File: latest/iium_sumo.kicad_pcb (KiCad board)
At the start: 2 copper layers, 101.3 x 62.2 mm, 60 parts, among them J1 I2C_VL53_1, J10 Cytron MD, J11 Cytron Start Module, J12 Conn_01x04, J13 Conn_01x04, J14 Conn_01x04, J15 EXTRA1, J16 Conn_01x02_Pin, J17 Conn_01x02_Pin, J18 UART1, J19 UART2, J2 I2C_VL53_2, J3 I2C_VL53_3, J4 I2C_VL53_4, J5 I2C_VL53_5, J6 IR_1, J7 IR_2, J8 IR_3, J9 IR_4, SW1 SW_SPST, SW2 SW_SPST, U1 TPS54360DDA, U4 Black Pill v2, U5 LM3940

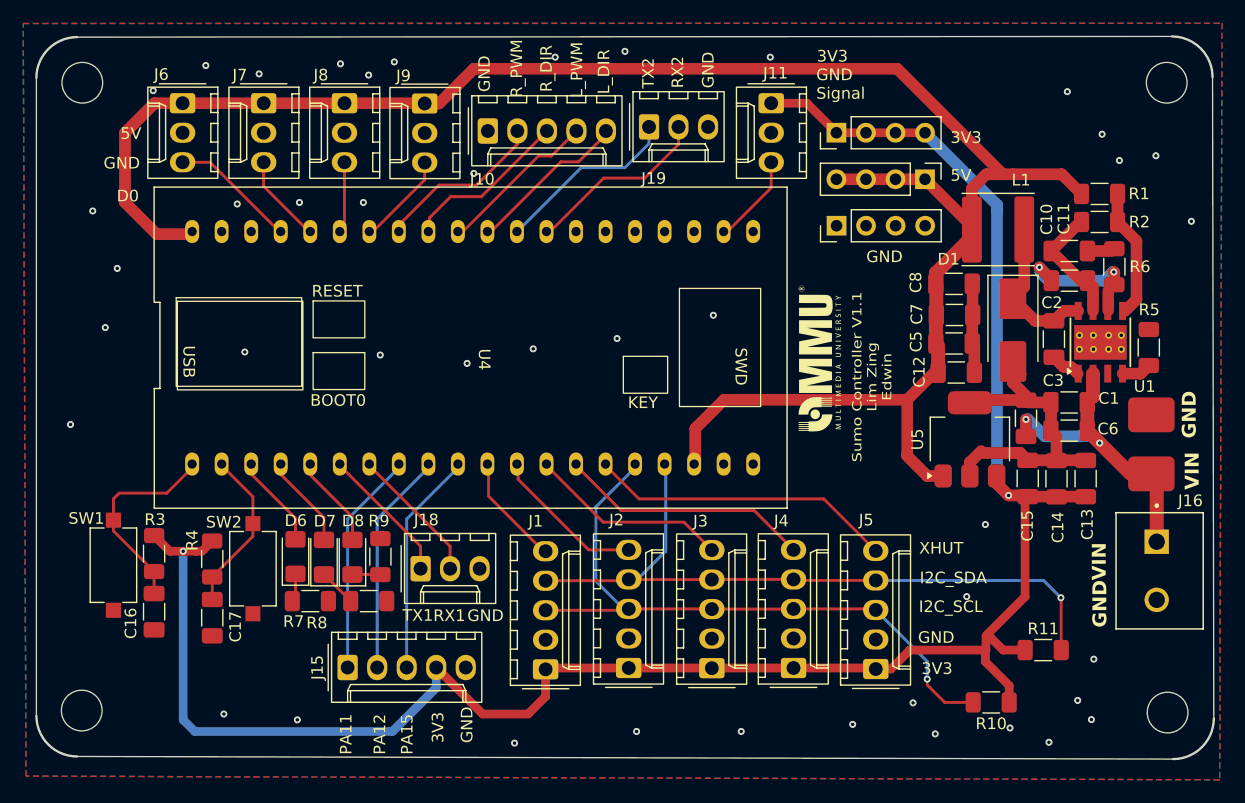
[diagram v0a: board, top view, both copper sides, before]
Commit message: Added Labels
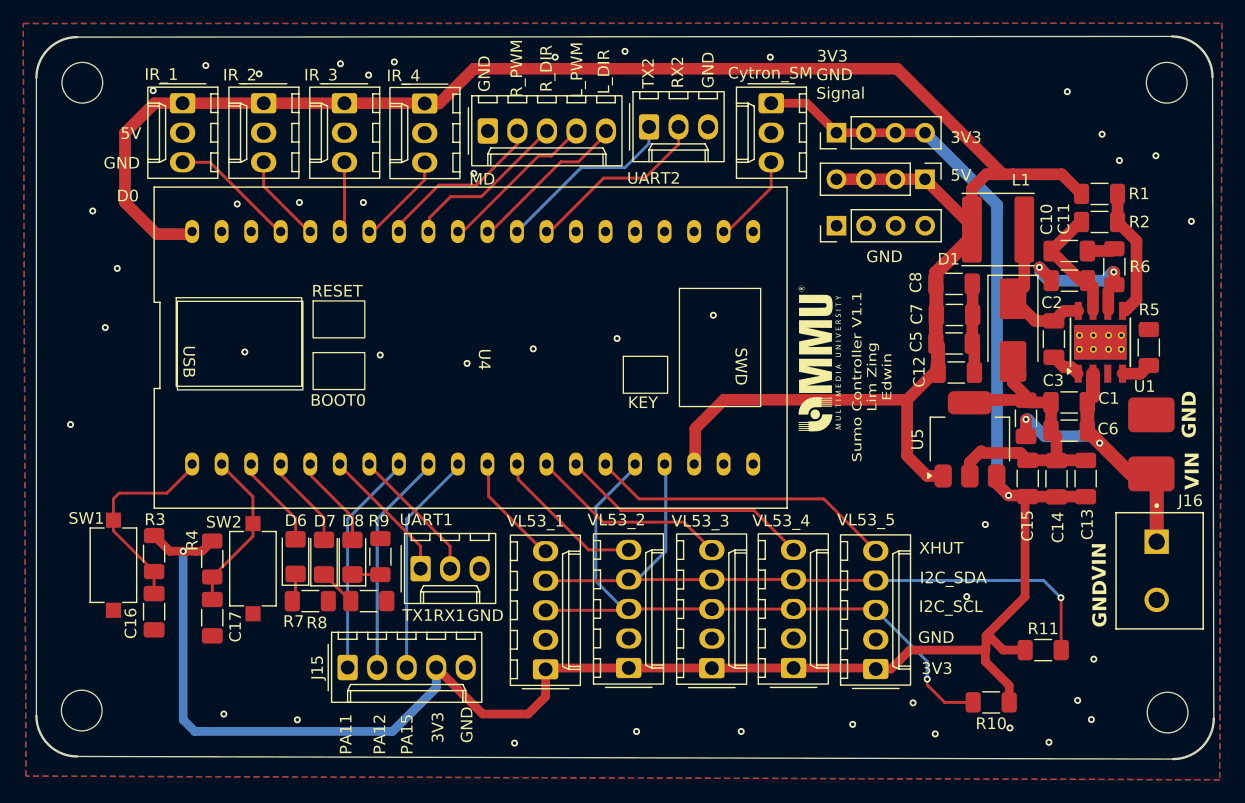
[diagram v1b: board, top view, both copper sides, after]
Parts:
- renumbered J11 to Cytron_SM, J6 to IR_1, J7 to IR_2, J8 to IR_3, J9 to IR_4, J10 to MD, J18 to UART1, J19 to UART2, J1 to VL53_1, J2 to VL53_2, J3 to VL53_3, J4 to VL53_4, J5 to VL53_5

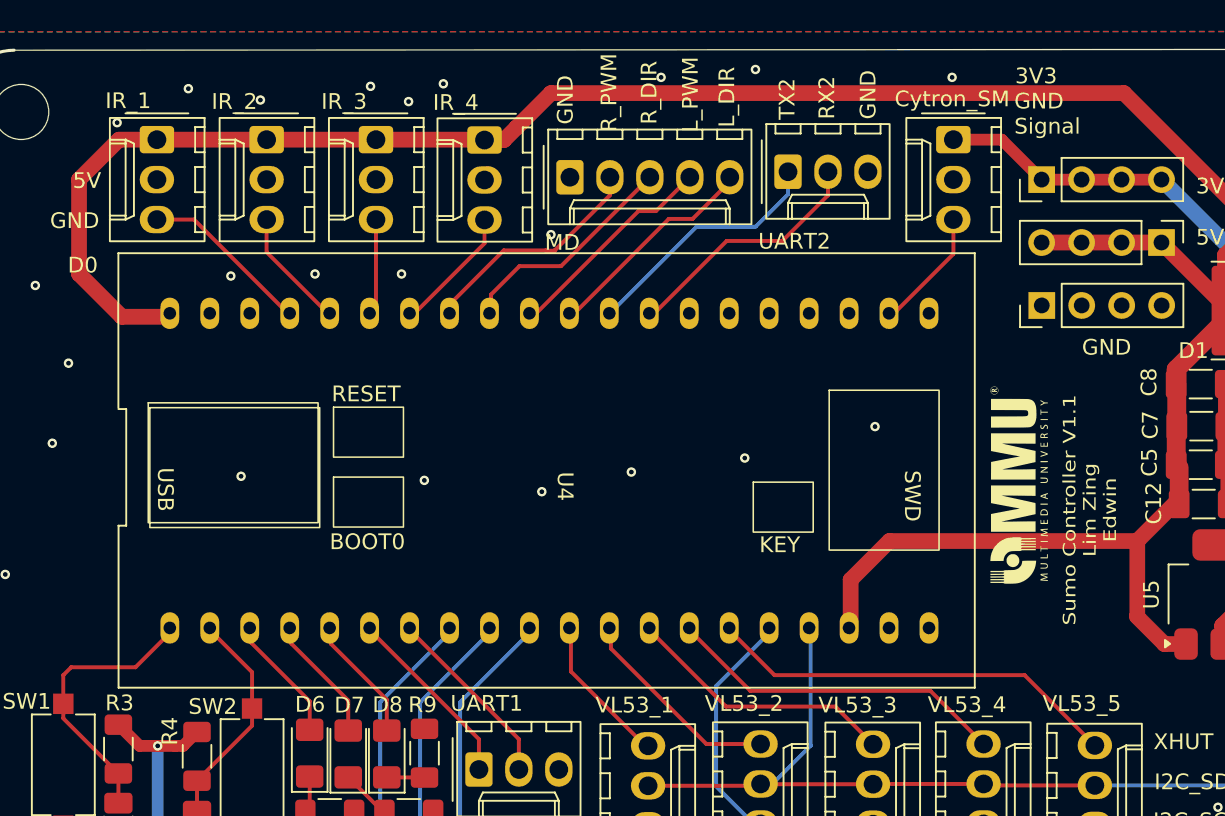
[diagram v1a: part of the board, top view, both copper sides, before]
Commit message: Updated pull resisto
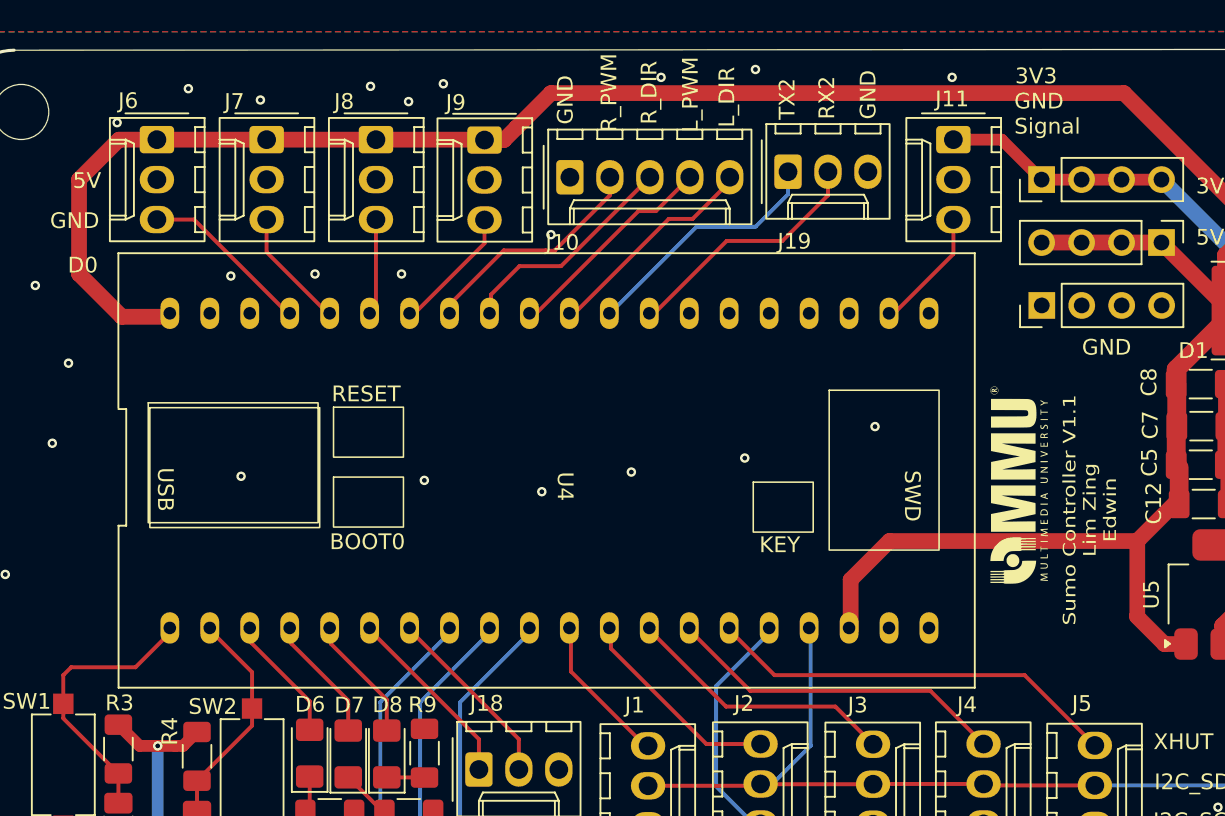
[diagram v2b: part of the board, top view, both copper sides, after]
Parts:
- R10, R11: value 4k -> 4.7k
- renumbered VL53_1 to J1, MD to J10, Cytron_SM to J11, UART1 to J18, UART2 to J19, VL53_2 to J2, VL53_3 to J3, VL53_4 to J4, VL53_5 to J5, IR_1 to J6, IR_2 to J7, IR_3 to J8, IR_4 to J9
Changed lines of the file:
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@@
 		(descr "Molex KK-254 Interconnect System, old/engineering part number: AE-6410-03A example for new part number: 22-27-2031, 3 Pins (http://www.molex.com/pdm_docs/sd/022272021_sd.pdf)")
 		(tags "connector Molex KK-254 vertical")
-		(property "Reference" "Cytron_SM"
+		(property "Reference" "J11"
 			(at -2.585 0.08 180)
 			(layer "F.SilkS")
@@
 		(descr "Molex KK-254 Interconnect System, old/engineering part number: AE-6410-05A example for new part number: 22-27-2051, 5 Pins (http://www.molex.com/pdm_docs/sd/022272021_sd.pdf)")
 		(tags "connector Molex KK-254 vertical")
-		(property "Reference" "VL53_2"
+		(property "Reference" "J2"
 			(at 12.73 -1.05 180)
 			(layer "F.SilkS")
@@
 		(descr "Molex KK-254 Interconnect System, old/engineering part number: AE-6410-05A example for new part number: 22-27-2051, 5 Pins (http://www.molex.com/pdm_docs/sd/022272021_sd.pdf)")
 		(tags "connector Molex KK-254 vertical")
-		(property "Reference" "VL53_3"
+		(property "Reference" "J3"
 			(at 12.645 -0.975 180)
 			(layer "F.SilkS")
@@
 			)
 		)
-		(property "Value" "4k"
+		(property "Value" "4.7k"
 			(at 0 1.83 0)
 			(layer "F.Fab")
@@
 		(descr "Molex KK-254 Interconnect System, old/engineering part number: AE-6410-05A example for new part number: 22-27-2051, 5 Pins (http://www.molex.com/pdm_docs/sd/022272021_sd.pdf)")
 		(tags "connector Molex KK-254 vertical")
-		(property "Reference" "VL53_1"
+		(property "Reference" "J1"
 			(at 12.745 -0.85 180)
 			(layer "F.SilkS")
@@
 		(descr "Molex KK-254 Interconnect System, old/engineering part number: AE-6410-05A example for new part number: 22-27-2051, 5 Pins (http://www.molex.com/pdm_docs/sd/022272021_sd.pdf)")
 		(tags "connector Molex KK-254 vertical")
-		(property "Reference" "VL53_5"
+		(property "Reference" "J5"
 			(at 12.82 -0.825 180)
 			(layer "F.SilkS")
@@
 			)
 		)
-		(property "Value" "4k"
+		(property "Value" "4.7k"
 			(at 0 1.83 0)
 			(layer "F.Fab")
@@
 		(descr "Molex KK-254 Interconnect System, old/engineering part number: AE-6410-05A example for new part number: 22-27-2051, 5 Pins (http://www.molex.com/pdm_docs/sd/022272021_sd.pdf)")
 		(tags "connector Molex KK-254 vertical")
-		(property "Reference" "MD"
+		(property "Reference" "J10"
 			(at -0.48 4.15 180)
 			(layer "F.SilkS")
@@
 		(descr "Molex KK-254 Interconnect System, old/engineering part number: AE-6410-03A example for new part number: 22-27-2031, 3 Pins (http://www.molex.com/pdm_docs/sd/022272021_sd.pdf)")
 		(tags "connector Molex KK-254 vertical")
-		(property "Reference" "IR_1"
+		(property "Reference" "J6"
 			(at -2.47 1.825 180)
 			(layer "F.SilkS")
@@
 		(descr "Molex KK-254 Interconnect System, old/engineering part number: AE-6410-03A example for new part number: 22-27-2031, 3 Pins (http://www.molex.com/pdm_docs/sd/022272021_sd.pdf)")
 		(tags "connector Molex KK-254 vertical")
-		(property "Reference" "UART1"
+		(property "Reference" "J18"
 			(at 0.49 -4.2 0)
 			(layer "F.SilkS")
@@
 		(descr "Molex KK-254 Interconnect System, old/engineering part number: AE-6410-03A example for new part number: 22-27-2031, 3 Pins (http://www.molex.com/pdm_docs/sd/022272021_sd.pdf)")
 		(tags "connector Molex KK-254 vertical")
-		(property "Reference" "IR_2"
+		(property "Reference" "J7"
 			(at -2.42 2.05 180)
 			(layer "F.SilkS")
@@
 		(descr "Molex KK-254 Interconnect System, old/engineering part number: AE-6410-03A example for new part number: 22-27-2031, 3 Pins (http://www.molex.com/pdm_docs/sd/022272021_sd.pdf)")
 		(tags "connector Molex KK-254 vertical")
-		(property "Reference" "IR_4"
+		(property "Reference" "J9"
 			(at -2.38 1.825 0)
 			(layer "F.SilkS")
@@
 		(descr "Molex KK-254 Interconnect System, old/engineering part number: AE-6410-03A example for new part number: 22-27-2031, 3 Pins (http://www.molex.com/pdm_docs/sd/022272021_sd.pdf)")
 		(tags "connector Molex KK-254 vertical")
-		(property "Reference" "IR_3"
+		(property "Reference" "J8"
 			(at -2.42 2.025 180)
 			(layer "F.SilkS")
@@
 		(descr "Molex KK-254 Interconnect System, old/engineering part number: AE-6410-05A example for new part number: 22-27-2051, 5 Pins (http://www.molex.com/pdm_docs/sd/022272021_sd.pdf)")
 		(tags "connector Molex KK-254 vertical")
-		(property "Reference" "VL53_4"
+		(property "Reference" "J4"
 			(at 12.655 -1.05 180)
 			(layer "F.SilkS")
@@
 		(descr "Molex KK-254 Interconnect System, old/engineering part number: AE-6410-03A example for new part number: 22-27-2031, 3 Pins (http://www.molex.com/pdm_docs/sd/022272021_sd.pdf)")
 		(tags "connector Molex KK-254 vertical")
-		(property "Reference" "UART2"
+		(property "Reference" "J19"
 			(at 0.405 4.425 0)
 			(layer "F.SilkS")

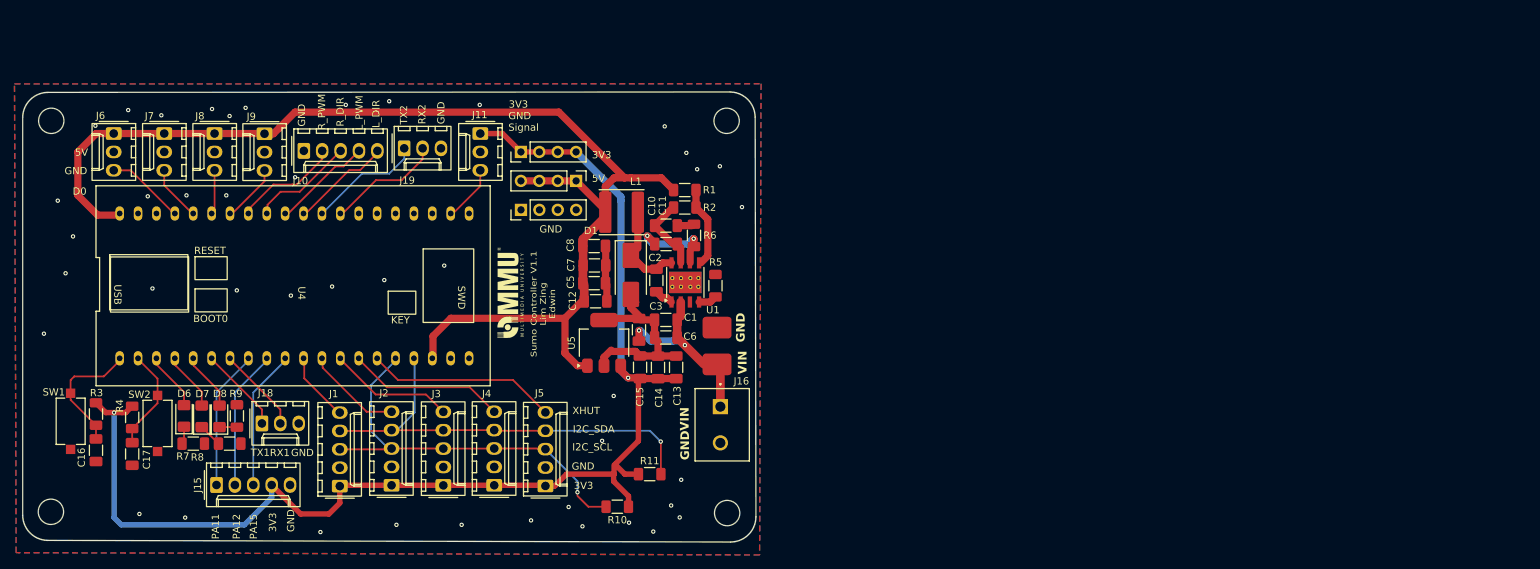
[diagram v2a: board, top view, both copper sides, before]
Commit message: pcb update and rearrange
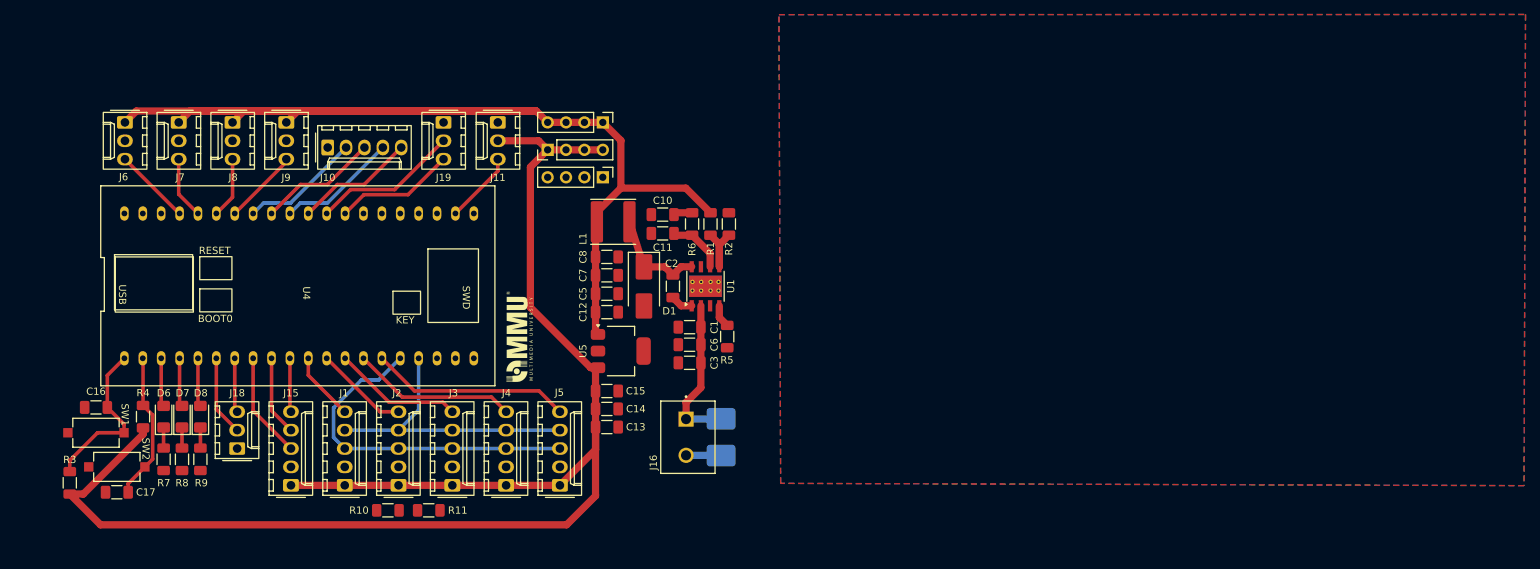
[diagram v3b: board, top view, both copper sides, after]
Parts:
- removed REF** (x4): MountingHole_3.5mm, MountingHole:MountingHole_3.5mm
- J17: moved to B.Cu
- moved R10 31.7 mm to (146.8, 118.0), turned to 0 degrees
- moved R11 30.9 mm to (152.5, 118.0), turned to 180 degrees
- moved C13 12.6 mm to (177.1, 106.5), turned to 0 degrees
- moved J14 12.2 mm to (176.5, 72.0), turned to -90 degrees
- moved J15 10.3 mm to (133.4, 114.5), turned to 90 degrees
- moved R3 10.2 mm to (102.9, 114.2), turned to 90 degrees
- moved C14 9.09 mm to (177.1, 104.0), turned to 0 degrees
- moved J13 8.88 mm to (176.5, 64.4)
- moved C3 8.35 mm to (188.5, 97.6), turned to 180 degrees
- moved SW2 8.22 mm to (109.4, 112.0), turned to 180 degrees
- moved R9 7.83 mm to (120.9, 111.0), turned to 90 degrees
- moved J17 7.54 mm to (192.8, 105.4), turned to -90 degrees
- moved R5 7.21 mm to (193.7, 94.0), turned to -90 degrees
- moved R8 6.93 mm to (118.4, 111.0), turned to 90 degrees
- moved R2 6.51 mm to (193.9, 78.5), turned to 90 degrees
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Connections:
- J11 pad 1: +3V3 -> GND
- J11 pad 2: GND -> +3V3
- J15 pad 1: /PA11 -> +3V3
- J15 pad 2: /PA12 -> GND
- J15 pad 3: /PA15 -> /PA11
- J15 pad 4: +3V3 -> /PA12
- J15 pad 5: GND -> /PA15
- J18 pad 1: /TX1 -> GND
- J18 pad 2: /RX1 -> /TX1
- J18 pad 3: GND -> /RX1
- J19 pad 1: /TX2 -> GND
- J19 pad 2: /RX2 -> /TX2
- J19 pad 3: GND -> /RX2
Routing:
- net +5V: track 170.8 -> 240.8 mm
- net GND: track 50.1 -> 4.85 mm, vias 43 -> 0
- net +3V3: track 180.3 -> 206.5 mm, vias 2 -> 0
- net /I2C_SDA: track 61.1 -> 41.1 mm, vias 1 -> 0
- net /PA15: track 19.1 -> 7.44 mm
- net /I2C_SCL: track 56.5 -> 48.0 mm, vias 1 -> 0
- net /PA12: track 19.1 -> 11.0 mm
- net /PB13: track 14.0 -> 20.5 mm
- net +36V: track 27.4 -> 21.3 mm, vias 2 -> 0
- net /PB12: track 17.6 -> 22.8 mm
- net COMP: track 12.6 -> 7.98 mm, vias 2 -> 0
- net /PA11: track 19.1 -> 14.6 mm
- net /TX2: track 15.9 -> 20.3 mm
- net /RX1: track 11.6 -> 7.52 mm
- net /LEFT_DIR: track 13.9 -> 16.8 mm
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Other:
- board outline removed
- board text removed: "3V3"
- board text removed: "5V"
- board text removed: "D0"
- board text removed: "GND"
- board text removed: "I2C_SCL"
- board text removed: "I2C_SDA"
- board text removed: "L_DIR"
- board text removed: "L_PWM"
- board text removed: "PA11"
- board text removed: "PA12"
- board text removed: "PA15"
- board text removed: "RX1"
- board text removed: "RX2"
- board text removed: "R_DIR"
- board text removed: "R_PWM"
- board text removed: "Signal"
- board text removed: "Sumo Controller V1.1 Lim Zing Edwin"
- board text removed: "TX1"
- board text removed: "TX2"
- board text removed: "VIN"
- board text removed: "XHUT"

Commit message: touch up
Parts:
- moved R10 25.4 mm to (148.5, 92.7), turned to -90 degrees
- moved R11 25.4 mm to (151.1, 92.7), turned to -90 degrees
- moved J13 7.60 mm to (176.5, 72.0), turned to 180 degrees
- moved J14 7.60 mm to (168.9, 72.0), turned to 180 degrees
- moved J12 5.39 mm to (172.7, 72.0), turned to 180 degrees
- moved J17 2.68 mm to (191.3, 103.1)
- moved J16 2.48 mm to (187.0, 105.6)
- moved D1 0.37 mm to (182.6, 87.1)
- moved R3 0.30 mm to (103.2, 114.2)
- moved R4 0.30 mm to (112.7, 105.1)
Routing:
- net +3V3: track 206.5 -> 253.6 mm
- net GND: track 4.85 -> 0.13 mm, vias 0 -> 45
- net +36V: track 21.3 -> 19.0 mm
- net +5V: track 240.8 -> 241.8 mm
- net /I2C_SDA: track 41.1 -> 41.6 mm

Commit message: drc cleared
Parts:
- removed G***: LOGO, shooter_foot_library:mmu_logo
- added REF**: MountingHole_3.5mm, MountingHole:MountingHole_3.5mm, F.Cu at (105.5, 65.5)
- added REF**: MountingHole_3.5mm, MountingHole:MountingHole_3.5mm, F.Cu at (194.5, 65.5)
- added REF**: MountingHole_3.5mm, MountingHole:MountingHole_3.5mm, F.Cu at (194.5, 114.5)
- added SW3: SW_SPDT, custom:SPDT_MT-1-102-A001-M200-RS, F.Cu at (189.3, 98.1)
- moved L1 14.2 mm to (185.0, 65.9), turned to 90 degrees
- moved J13 7.81 mm to (177.5, 64.3), turned to 0 degrees
- moved C13 6.88 mm to (178.3, 99.7)
- moved C14 6.88 mm to (178.3, 97.2)
- moved C15 6.88 mm to (178.3, 94.7)
- moved D1 6.79 mm to (183.4, 80.3)
- moved U5 6.53 mm to (179.9, 89.5)
- moved C7 6.32 mm to (177.9, 79.3)
- moved C12 6.32 mm to (177.9, 84.4)
- moved C5 6.32 mm to (177.9, 81.8)
- moved C8 6.32 mm to (177.9, 76.7)
- moved R1 5.74 mm to (192.4, 72.8)
- moved R2 5.74 mm to (194.9, 72.8)
- moved R6 5.74 mm to (189.8, 72.8)
- moved C1 5.74 mm to (189.5, 87.1)
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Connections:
- C1 pad 1: +36V -> Net-(SW3-B)
- C3 pad 1: +36V -> Net-(SW3-B)
- C6 pad 1: +36V -> Net-(SW3-B)
- J16 pad 1: +36V -> GND
- J16 pad 2: GND -> +36V
- J17 pad 1: +36V -> GND
- J17 pad 2: GND -> +36V
- U1 pad 2: +36V -> Net-(SW3-B)
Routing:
- net +5V: track 241.8 -> 156.7 mm
- net Net-(SW3-B): track 0.00 -> 14.7 mm
- net +36V: track 19.0 -> 11.4 mm
- net /I2C_SDA: track 41.6 -> 49.0 mm
- net /I2C_SCL: track 47.9 -> 55.2 mm
- net +3V3: track 253.6 -> 260.7 mm
- net Net-(D1-K): track 14.4 -> 20.2 mm
- net /PB12: track 22.7 -> 20.9 mm
- net /LEFT_DIR: track 16.8 -> 18.6 mm
- net /IR4_D0: track 10.5 -> 12.0 mm
- net /RIGHT_PWM: track 16.9 -> 18.4 mm
- net /LEFT_PWM: track 17.0 -> 18.5 mm
- net /TX2: track 20.3 -> 21.8 mm
- net /RX2: track 16.7 -> 18.2 mm
- net /RIGHT_DIR: track 17.1 -> 18.4 mm
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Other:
- board outline added: 100 x 60 mm
